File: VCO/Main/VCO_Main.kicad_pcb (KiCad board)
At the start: 2 copper layers, 43.2 x 92.7 mm, 59 parts, among them J1 Conn_01x14, J3 Power, U1 AS3340, U5 LM13700, U6 TL072, U7 TL072

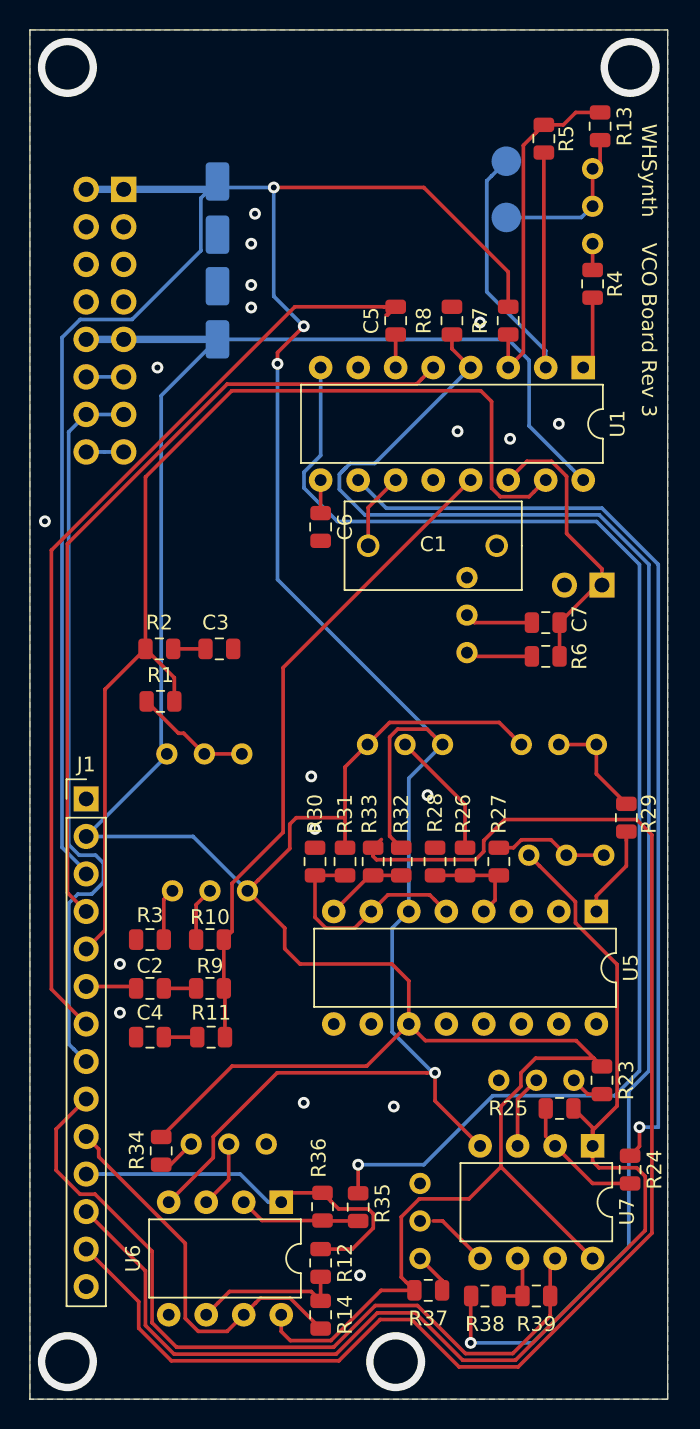
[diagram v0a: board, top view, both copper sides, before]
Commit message: Resolve most of the issues in known_issues.txt
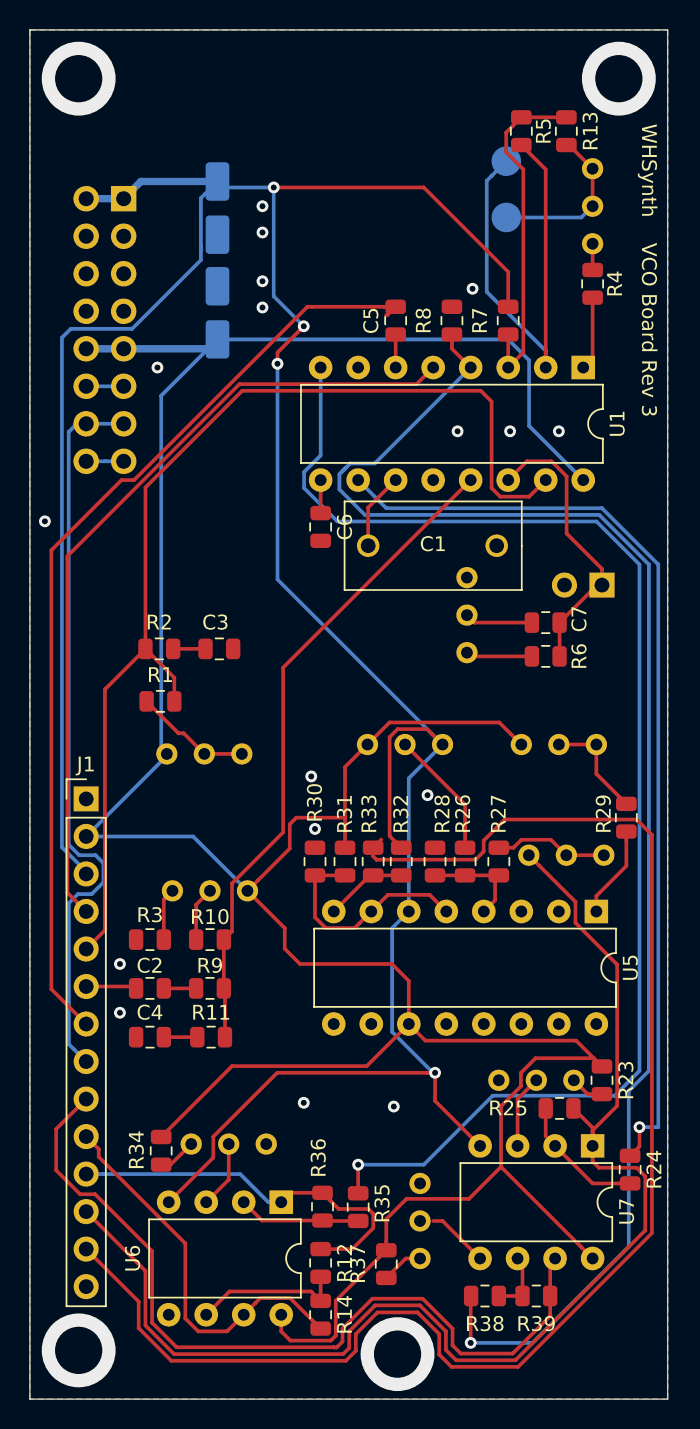
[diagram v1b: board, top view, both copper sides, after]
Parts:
- moved R37 3.35 mm to (91.4, 150.9), turned to 270 degrees
- moved R13 2.31 mm to (103.6, 74.2)
- moved R5 1.61 mm to (100.6, 74.2)
- moved J3 0.63 mm to (73.7, 78.7)
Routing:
- net /Sine: track 98.0 -> 99.9 mm
- net /Tri: track 84.8 -> 86.6 mm
- net -12V: track 197.3 -> 199.0 mm
- net /Pulse: track 55.1 -> 56.7 mm
- net Net-(R5-Pad2): track 30.8 -> 32.1 mm
- net +12V: track 216.6 -> 215.3 mm
- net GNDREF: vias 22 -> 21

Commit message: Fix minor issues with VCO board
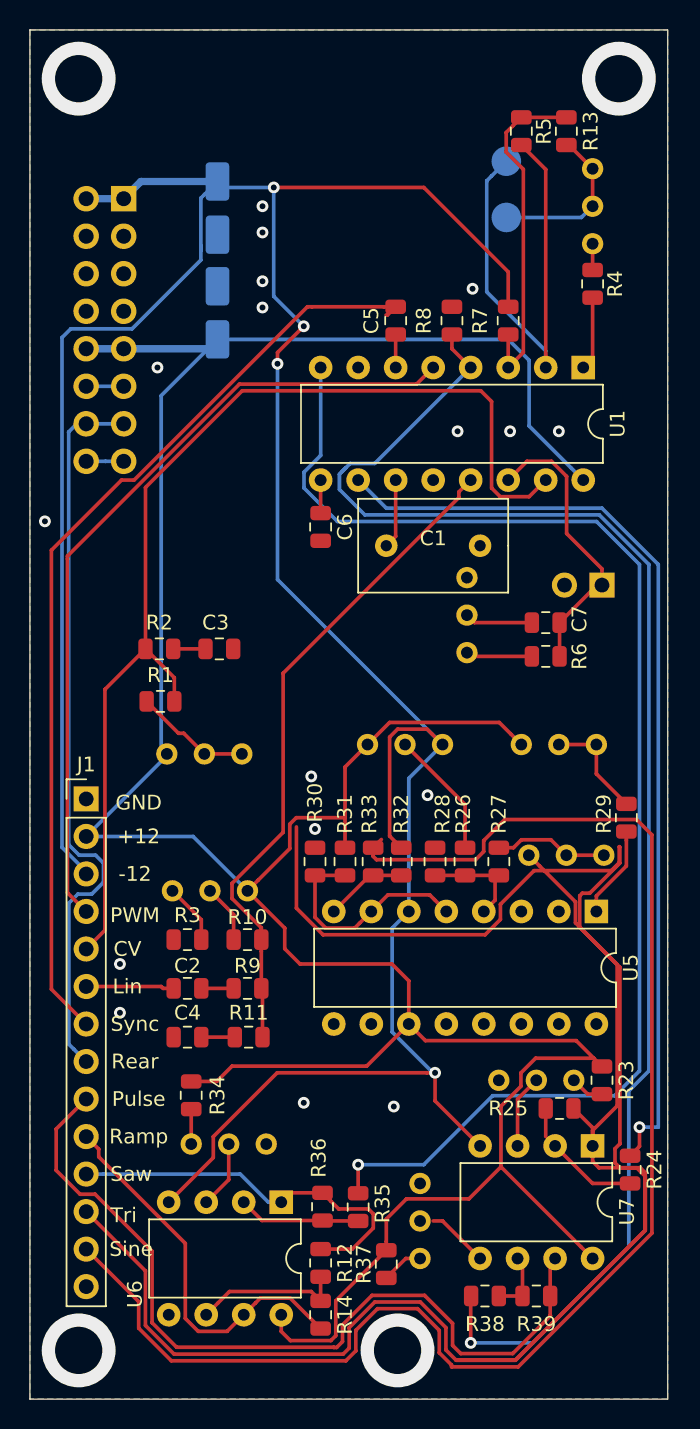
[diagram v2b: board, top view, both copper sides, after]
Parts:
- added REF**: OSHW-Logo2_7.3x6mm_SilkScreen, Symbol:OSHW-Logo2_7.3x6mm_SilkScreen, B.Cu at (90.7, 77.5)
- C1: footprint AS3340_VCO:Mica_cap -> Eurorack:Mica_Cap
- moved R34 4.28 mm to (78.2, 139.4)
- moved R10 2.54 mm to (82.0, 128.9)
- moved R11 2.54 mm to (82.1, 135.5)
- moved R9 2.54 mm to (82.0, 132.2)
- moved C2 2.54 mm to (78.0, 132.2)
- moved C4 2.54 mm to (78.0, 135.5)
- moved R3 2.54 mm to (78.0, 128.9)
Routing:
- net /Tri: track 86.6 -> 165.7 mm
- net +12V: track 215.3 -> 211.7 mm
- net /LIN: track 3.43 -> 5.97 mm
- net Net-(R10-Pad1): track 44.7 -> 45.3 mm
- net Net-(R3-Pad2): track 3.54 -> 4.11 mm
- net /Pulse: track 56.7 -> 57.2 mm
- net /Sine: track 99.9 -> 100.4 mm
- net Net-(C1-Pad2): track 5.22 -> 4.71 mm
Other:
- board text added: "VCO Main Board Rev 3"
- board text added: "WH"
- board text removed: "VCO Board Rev 3"
- board text removed: "WHSynth"

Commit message: Bunch of bug fixes and tweaks
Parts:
- added H1: Top_MH1, Eurorack:eurorack_mounting_hole, F.Cu at (70.6, 70.6)
- added H2: Bottom_MH1, Eurorack:eurorack_mounting_hole, F.Cu at (70.6, 156.7)
- added H3: Top_MH2, Eurorack:eurorack_mounting_hole, F.Cu at (107.2, 70.6)
- added H4: Bottom_MH2, Eurorack:eurorack_mounting_hole, F.Cu at (92.2, 156.7)
- R25: value 10K -> 20K
- R35: value 20K -> 10K
- R38: value 24K -> 12K
- R39: value 9.1K -> 10K
- moved J3 18.0 mm to (71.1, 96.5), turned to 0 degrees
- moved C9 16.4 mm to (80.8, 95.8), turned to 270 degrees
- moved RV3 3.59 mm to (99.4, 106.9), turned to 0 degrees
- moved C8 1.61 mm to (80.8, 87.9), turned to 270 degrees
- moved JP5 0.38 mm to (106.4, 104.9)
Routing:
- net /Tri: track 165.7 -> 115.1 mm
- net -12V: track 199.0 -> 182.5 mm
- net /REAR_CV: track 50.5 -> 60.6 mm
- net +12V: track 211.7 -> 205.8 mm
- net GNDREF: track 4.61 -> 0.72 mm, vias 21 -> 11
- net Net-(R6-Pad1): track 4.50 -> 3.61 mm
- net Net-(C7-Pad2): track 19.5 -> 20.3 mm

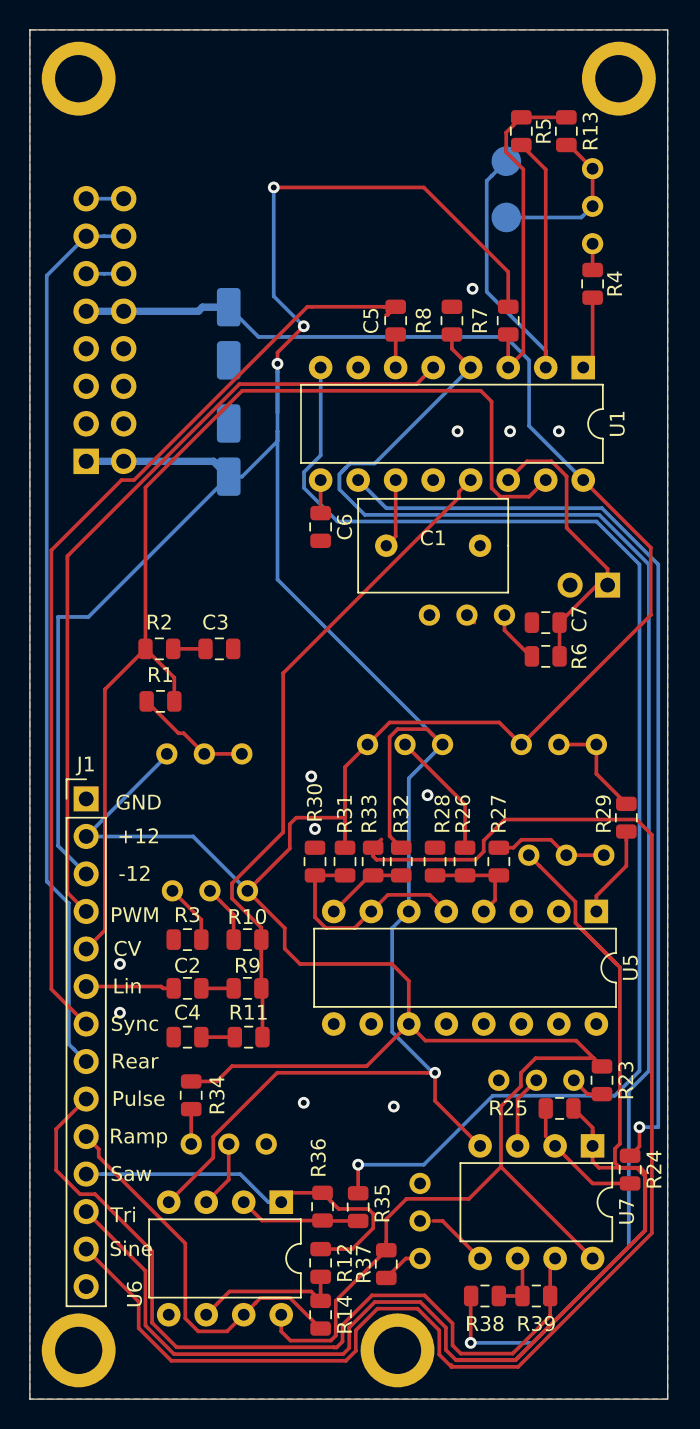
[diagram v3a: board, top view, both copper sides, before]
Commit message: Clean up layout of VCO board
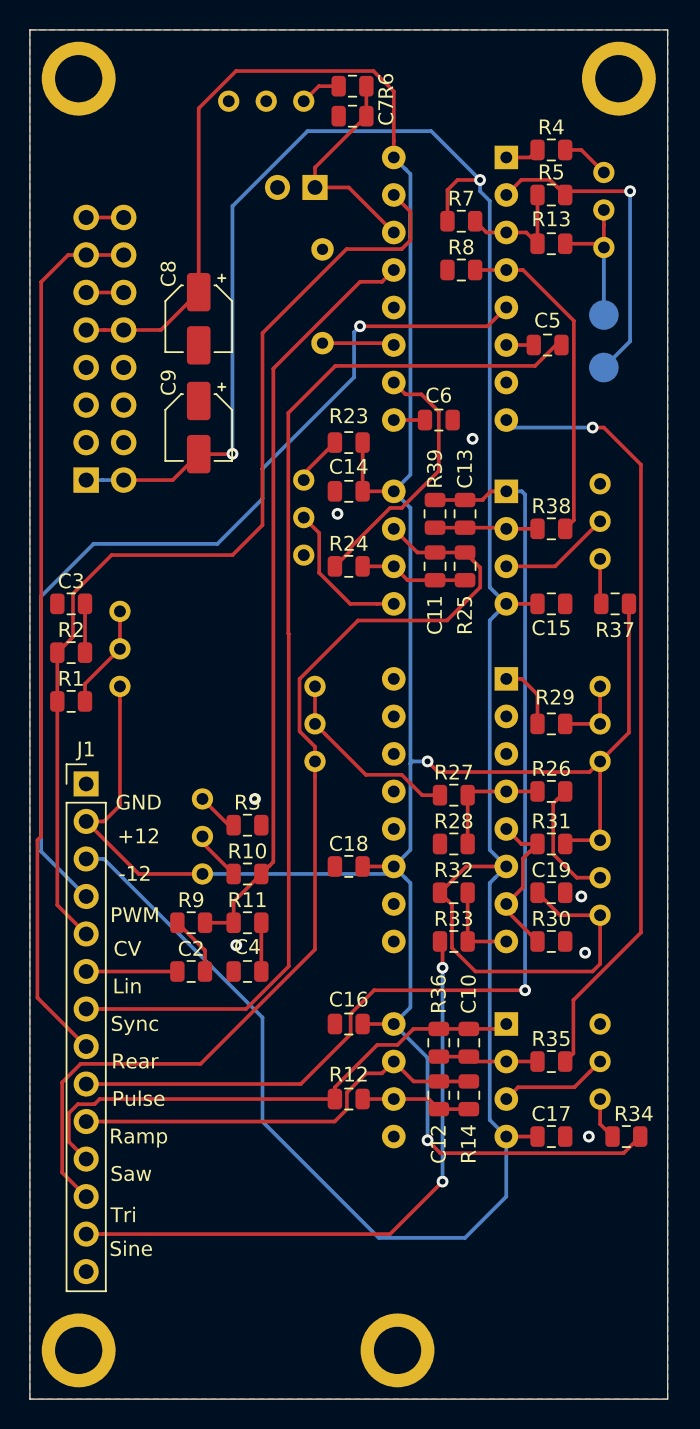
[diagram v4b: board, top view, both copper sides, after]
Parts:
- added C10: C, Capacitor_SMD:C_0805_2012Metric, F.Cu at (97.0, 135.9)
- added C11: C, Capacitor_SMD:C_0805_2012Metric, F.Cu at (94.7, 103.6)
- added C12: C, Capacitor_SMD:C_0805_2012Metric, F.Cu at (95.0, 139.4)
- added C13: C, Capacitor_SMD:C_0805_2012Metric, F.Cu at (96.8, 100.1)
- added C14: 0.1uF, Capacitor_SMD:C_0805_2012Metric, F.Cu at (88.9, 98.6)
- added C15: 0.1uF, Capacitor_SMD:C_0805_2012Metric, F.Cu at (102.6, 106.2)
- added C16: 0.1uF, Capacitor_SMD:C_0805_2012Metric, F.Cu at (88.9, 134.6)
- added C17: 0.1uF, Capacitor_SMD:C_0805_2012Metric, F.Cu at (102.6, 142.2)
- added C18: 0.1uF, Capacitor_SMD:C_0805_2012Metric, F.Cu at (88.9, 124.0)
- added C19: 0.1uF, Capacitor_SMD:C_0805_2012Metric, F.Cu at (102.6, 125.7)
- C1, U1, U5, U6, U7: moved to B.Cu
- C8, C9: moved to F.Cu
- moved REF** 79.9 mm to (79.0, 156.5)
- moved R39 53.4 mm to (94.7, 100.1), turned to 90 degrees
- moved R38 52.1 mm to (102.6, 101.1), turned to 180 degrees
- moved RV11 48.9 mm to (105.9, 103.1)
- moved R37 47.3 mm to (106.9, 106.2), turned to 180 degrees
- moved R23 46.5 mm to (88.9, 95.2), turned to 180 degrees
- moved R24 45.1 mm to (88.9, 103.6), turned to 0 degrees
- moved U7 44.7 mm to (99.6, 98.6), turned to 180 degrees
- moved RV6 44.6 mm to (85.9, 97.8), turned to 90 degrees
- moved R6 40.8 mm to (89.2, 71.1)
- moved RV3 37.4 mm to (85.9, 72.1)
- moved R25 37.3 mm to (96.8, 103.6), turned to 90 degrees
- moved C7 36.7 mm to (89.2, 73.2)
- moved JP5 33.4 mm to (86.6, 78.0)
- moved R34 29.6 mm to (107.7, 142.2), turned to 180 degrees
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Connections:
- R24 pad 2: Net-(R24-Pad2) -> Net-(C11-Pad2)
- R25 pad 1: Net-(R24-Pad2) -> Net-(C11-Pad2)
- R38 pad 2: Net-(R38-Pad2) -> Net-(C13-Pad2)
- R39 pad 1: Net-(R38-Pad2) -> Net-(C13-Pad2)
- U7 pad 1: /Tri -> /Pulse
- U7 pad 2: Net-(R24-Pad2) -> Net-(C13-Pad2)
- U7 pad 3: Net-(RV6-Pad2) -> Net-(RV11-Pad2)
- U7 pad 5: Net-(RV11-Pad2) -> Net-(RV6-Pad2)
- U7 pad 6: Net-(R38-Pad2) -> Net-(C11-Pad2)
- U7 pad 7: /Pulse -> /Tri
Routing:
- net /Output Conditioning/RAW_PULSE: track 102.5 -> 22.4 mm, vias 1 -> 0
- net /Sine: track 100.5 -> 41.9 mm, vias 0 -> 2
- net /Output Conditioning/RAW_TRI: track 64.3 -> 17.7 mm, vias 1 -> 0
- net /Tri: track 115.1 -> 71.1 mm
- net /Output Conditioning/RAW_RAMP: track 91.4 -> 52.9 mm
- net -12V: track 182.5 -> 201.7 mm, vias 4 -> 2
- net /Pulse: track 57.2 -> 73.2 mm, vias 0 -> 1
- net /Vee: track 23.6 -> 8.15 mm
- net Net-(R5-Pad2): track 32.1 -> 22.0 mm, vias 0 -> 1
- net /Saw: track 26.2 -> 36.2 mm
- net /PWM: track 54.6 -> 64.2 mm, vias 0 -> 1
- net /SYNC: track 64.1 -> 72.8 mm
- net Net-(R24-Pad2): track 8.04 -> 0.00 mm
- net Net-(C11-Pad2): track 0.00 -> 7.32 mm
- net Net-(C13-Pad2): track 0.00 -> 6.97 mm
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
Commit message: Added Gerber files
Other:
- board text added: "+12V"
- board text added: "-12V"
- board text removed: "+12"
- board text removed: "-12"
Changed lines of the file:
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@@
   (general
     (thickness 1.6)
-    (drawings 29)
+    (drawings 30)
     (tracks 363)
     (zones 0)
@@
     )
   )
+  (gr_text GND (at 74.168 151.384) (layer F.SilkS)
+    (effects (font (size 1 1) (thickness 0.15)))
+  )
   (gr_text WH (at 108.458 158.496) (layer B.SilkS)
     (effects (font (size 1 1) (thickness 0.15)) (justify mirror))
@@
     (effects (font (size 1 1) (thickness 0.15)) (justify mirror))
   )
-  (gr_text Ramp (at 74.676 142.24) (layer F.SilkS)
+  (gr_text Ramp (at 74.676 141.224) (layer F.SilkS)
     (effects (font (size 1 1) (thickness 0.15)))
   )
@@
   (gr_line (start 67.31 67.31) (end 67.31 160.02) (layer Edge.Cuts) (width 0.05))
   (gr_line (start 67.31 67.31) (end 110.49 67.31) (layer Edge.Cuts) (width 0.05))
-  (gr_text GND (at 74.676 119.634) (layer F.SilkS)
+  (gr_text GND (at 74.422 118.364) (layer F.SilkS)
     (effects (font (size 1 1) (thickness 0.15)))
   )
@@
     (effects (font (size 1 1) (thickness 0.15)) (justify mirror))
   )
-  (gr_text Sine (at 74.168 149.86) (layer F.SilkS)
+  (gr_text Sine (at 74.168 148.844) (layer F.SilkS)
     (effects (font (size 1 1) (thickness 0.15)))
   )
-  (gr_text Tri (at 73.66 147.574) (layer F.SilkS)
+  (gr_text Tri (at 73.66 146.304) (layer F.SilkS)
     (effects (font (size 1 1) (thickness 0.15)))
   )
-  (gr_text Pulse (at 74.676 139.7) (layer F.SilkS)
+  (gr_text Pulse (at 74.676 138.684) (layer F.SilkS)
     (effects (font (size 1 1) (thickness 0.15)))
   )
-  (gr_text Saw (at 74.168 144.78) (layer F.SilkS)
+  (gr_text Saw (at 74.168 143.764) (layer F.SilkS)
     (effects (font (size 1 1) (thickness 0.15)))
   )
@@
     (effects (font (size 1 1) (thickness 0.15)) (justify mirror))
   )
-  (gr_text -12 (at 74.422 124.46) (layer F.SilkS)
+  (gr_text -12V (at 74.676 123.444) (layer F.SilkS)
     (effects (font (size 1 1) (thickness 0.15)))
   )
-  (gr_text +12 (at 74.676 121.92) (layer F.SilkS)
+  (gr_text +12V (at 74.676 120.904) (layer F.SilkS)
     (effects (font (size 1 1) (thickness 0.15)))
   )
-  (gr_text CV (at 73.914 129.54) (layer F.SilkS)
+  (gr_text CV (at 73.914 128.524) (layer F.SilkS)
     (effects (font (size 1 1) (thickness 0.15)))
   )
-  (gr_text Lin (at 73.914 132.08) (layer F.SilkS)
+  (gr_text Lin (at 73.914 131.064) (layer F.SilkS)
     (effects (font (size 1 1) (thickness 0.15)))
   )
-  (gr_text Rear (at 74.422 137.16) (layer F.SilkS)
+  (gr_text Rear (at 74.422 136.144) (layer F.SilkS)
     (effects (font (size 1 1) (thickness 0.15)))
   )
-  (gr_text "Sync\n" (at 74.422 134.62) (layer F.SilkS)
+  (gr_text "Sync\n" (at 74.422 133.604) (layer F.SilkS)
     (effects (font (size 1 1) (thickness 0.15)))
   )
-  (gr_text PWM (at 74.422 127.254) (layer F.SilkS)
+  (gr_text PWM (at 74.422 126.238) (layer F.SilkS)
     (effects (font (size 1 1) (thickness 0.15)))
   )
